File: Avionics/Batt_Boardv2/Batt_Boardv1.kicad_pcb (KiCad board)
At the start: 2 copper layers, 43 parts, among them J3 Screw_Terminal_01x01, J4 JST_PH_S2B-PH-SM4, J5 Screw_Terminal_01x02, J6 Screw_Terminal_01x02, J7 Screw_Terminal_01x02, J8 Screw_Terminal_01x02, Q1 IRF7458, Q2 IRF7458, U3 TMP36xS

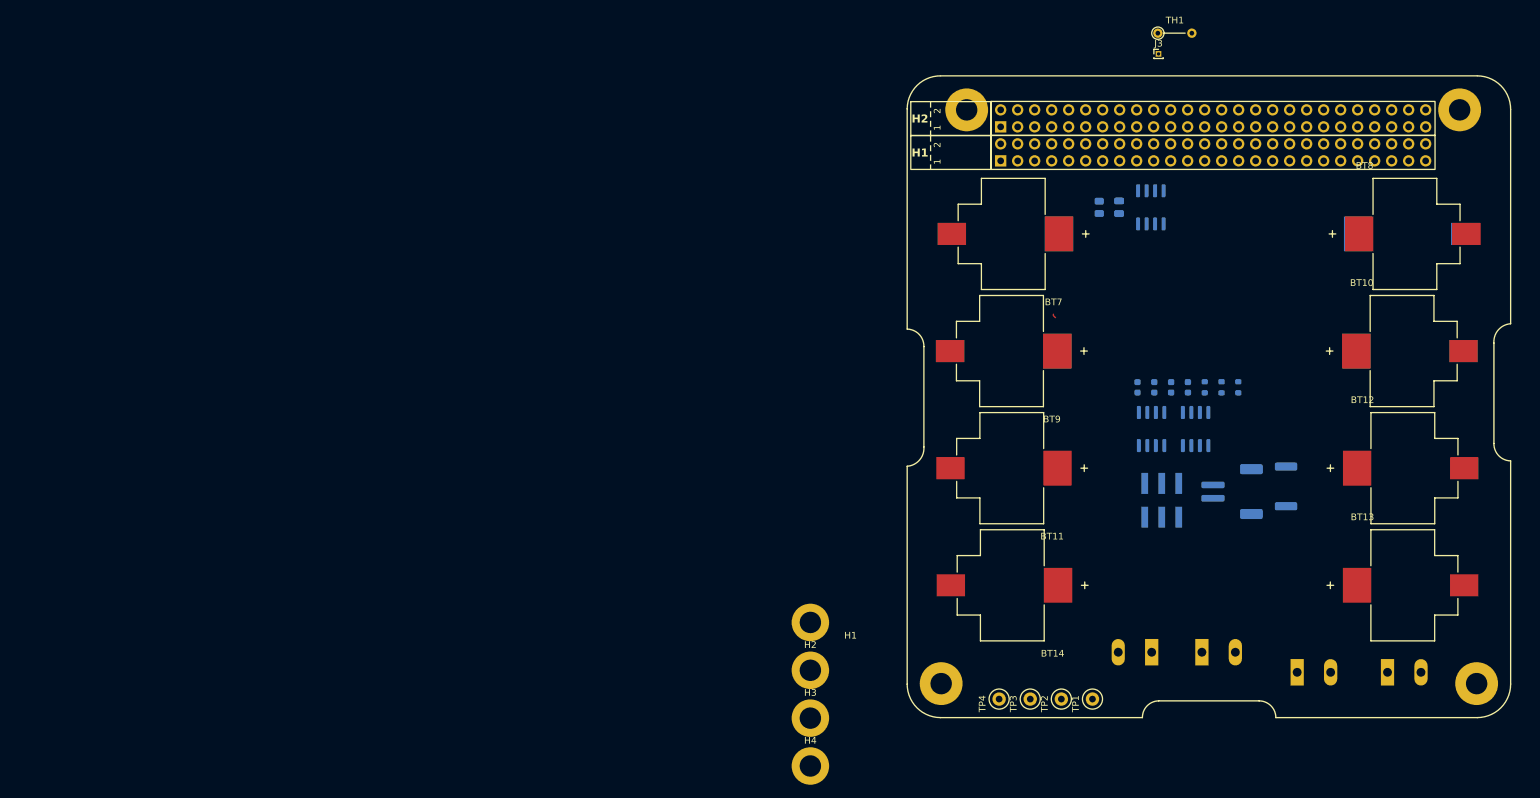
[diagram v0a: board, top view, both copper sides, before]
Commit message: 12/3/2024, Sephora Poteau: changed PC104 layout to include copper layer and edge cuts, and changed placement of components on Batt_Boardv2
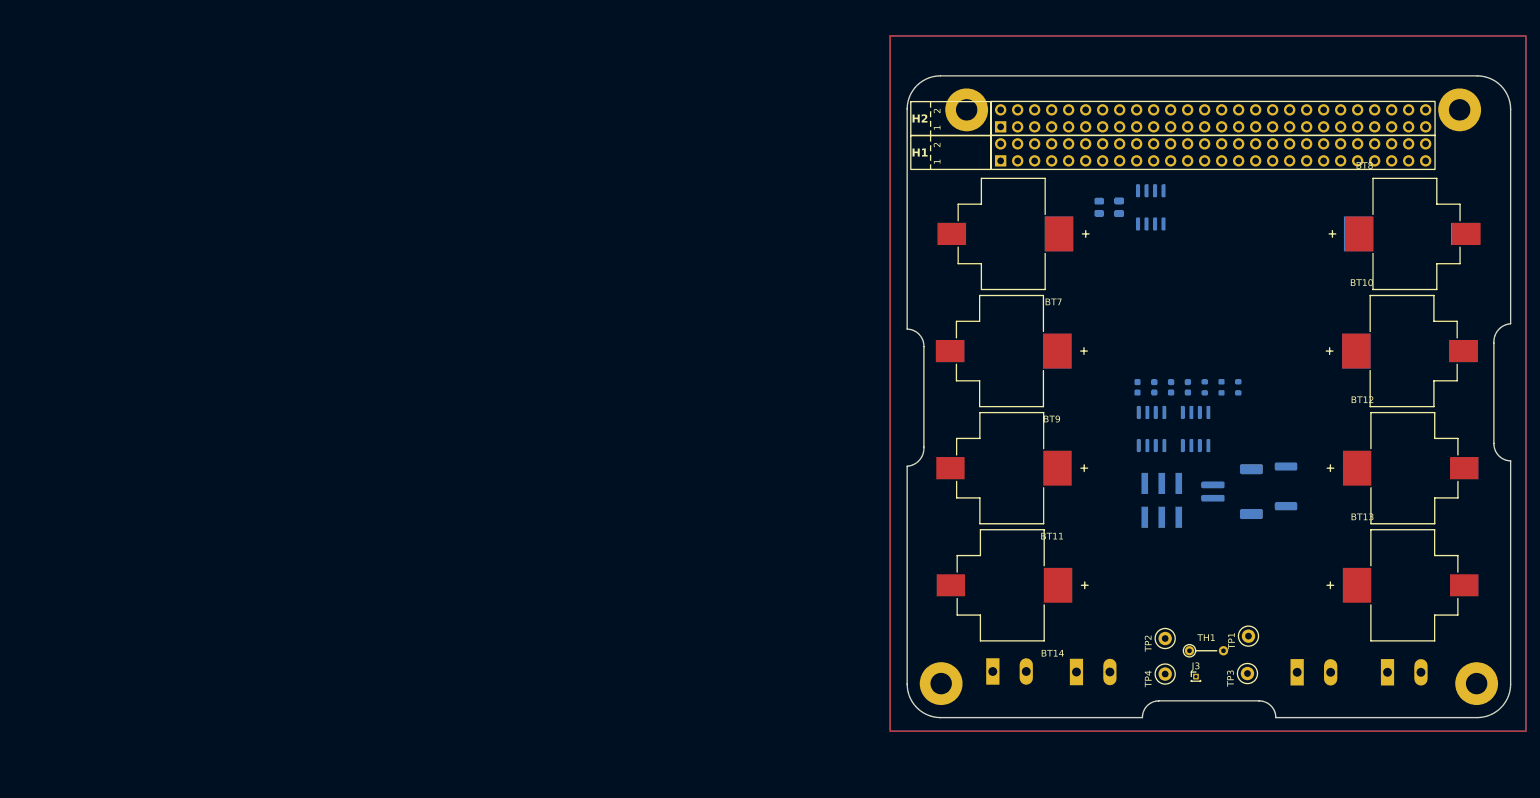
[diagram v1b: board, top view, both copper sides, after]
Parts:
- removed H1, H2, H3, H4: MountingHole_Pad, MountingHole:MountingHole_3.2mm_M3_DIN965_Pad
- moved J3 93.2 mm to (207.1, 139.1)
- moved TH1 92.4 mm to (206.1, 135.3)
- moved TP3 32.7 mm to (214.8, 138.7)
- moved TP1 25.1 mm to (215.0, 133.1)
- moved TP4 25.1 mm to (202.5, 138.8)
- moved J5 23.9 mm to (176.8, 138.4), turned to 0 degrees
- moved J8 19.0 mm to (189.3, 138.5)
- moved TP2 18.0 mm to (202.5, 133.5)
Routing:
- net (no net): track 1.56 -> 0.00 mm
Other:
- board outline added: 90.2 x 95.9 mm

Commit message: meeting
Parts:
- removed D1: TEMP_PWR, LED_SMD:LED_0805_2012Metric
- removed J3: Screw_Terminal_01x01, Connector_PinHeader_1.00mm:PinHeader_1x01_P1.00mm_Vertical
- removed J4: JST_PH_S2B-PH-SM4, Connector_JST:JST_PH_S2B-PH-SM4-TB_1x02-1MP_P2.00mm_Horizontal
- removed J5, J6, J7, J8: Screw_Terminal_01x02, TerminalBlock:TerminalBlock_Altech_AK300-2_P5.00mm
- removed R2: 15, Resistor_SMD:R_0805_2012Metric
- removed R5460N233AF1: ~, Connector_PinHeader_2.54mm:PinHeader_2x03_P2.54mm_Vertical_SMD
- removed TH1: Thermistor, Resistor_THT:R_Axial_DIN0204_L3.6mm_D1.6mm_P5.08mm_Vertical
- added S-8252: ~, Package_TO_SOT_SMD:SOT-23-5, B.Cu at (200.3, 121.3)
- C1, C3, C4, C5: footprint Capacitor_SMD:C_0603_1608Metric -> Capacitor_SMD:C_0805_2012Metric
- R1: footprint Resistor_SMD:R_2512_6332Metric -> Package_TO_SOT_SMD:TO-263-2
- R4, R5: footprint Resistor_SMD:R_0603_1608Metric -> Resistor_SMD:R_0805_2012Metric
- moved U3 63.1 mm to (195.9, 132.0)
- moved C2 61.9 mm to (204.8, 130.3)
- moved TP1 20.4 mm to (233.5, 141.5)
- moved TP2 19.7 mm to (184.5, 141.5)
- moved TP3 10.1 mm to (224.5, 141.5)
- moved C1 9.15 mm to (195.8, 104.7)
- moved C3 9.15 mm to (198.3, 104.7)
- moved C4 9.15 mm to (200.8, 104.7)
- moved C5 9.15 mm to (203.3, 104.7)
- moved Q1 9.15 mm to (197.9, 110.9)
- moved Q2 9.15 mm to (204.5, 110.9)
- moved R3 9.15 mm to (205.8, 104.7)
- moved R4 9.15 mm to (208.4, 104.7)
- moved R5 9.15 mm to (210.9, 104.7)
- moved TP4 8.94 mm to (194.0, 141.5)
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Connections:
- C1 pad 2: /Pack - -> GND
- C2 pad 1: Net-(D1-A) -> /3V3
- Q2 pad 1: /Pack - -> GND
- Q2 pad 2: /Pack - -> GND
- Q2 pad 3: /Pack - -> GND
- R3 pad 2: /Pack - -> GND
- TP3 pad 1: /Pack - -> GND
- TP4 pad 1: /Pack + -> /BATT_CS
- U1 pad 10: unconnected-(U1-Pad10) -> /BATT_CS
- U1 pad 11: unconnected-(U1-Pad11) -> /BATT_CS
- U1 pad 12: unconnected-(U1-BGLBON_RST-Pad12) -> /BATT_CS
- U1 pad 53: /batt_board_temp -> unconnected-(U1-TEMP_1-Pad53)
- U1 pad 57: unconnected-(U1-TEMP_7-Pad57) -> /batt_board_temp
- U1 pad 79: unconnected-(U1-3V3_MAIN-Pad79) -> /3V3
- U1 pad 80: unconnected-(U1-3V3_MAIN-Pad80) -> /3V3
- U1 pad 81: unconnected-(U1-GND-Pad81) -> GND
- U1 pad 82: unconnected-(U1-GND-Pad82) -> GND
- U1 pad 83: unconnected-(U1-GND-Pad83) -> GND
- U1 pad 84: unconnected-(U1-GND-Pad84) -> GND
- U1 pad 9: unconnected-(U1-Pad9) -> /BATT_CS
- U3 pad 5: Net-(D1-A) -> /3V3
- U3 pad 8: Net-(D1-A) -> /3V3

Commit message: feat: batt & PDU progress
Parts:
- removed BT10, BT11, BT12, BT13, BT14, BT15, BT17, BT18, BT7, BT8, BT9: 54, Battery 54:BAT_254TR
- removed U1: ~, PC104:PC104ConnectorFootprint (1)
- added BT1: 54, 254:BAT_254_1, B.Cu at (75.2, 68.1)
- added BT2: 54, 254:BAT_254_1, B.Cu at (75.2, 86.4)
- added BT3: 54, 254:BAT_254_1, B.Cu at (75.2, 104.8)
- added BT4: 54, 254:BAT_254_1, B.Cu at (74.9, 123.2)
- added BT5: 54, 254:BAT_254_1, F.Cu at (75.9, 68.1)
- added G***: LOGO, LOGO, F.Cu at (100.8, 129.9)
- added H1: MountingHole, MountingHole:MountingHole_3.2mm_M3_Pad_TopBottom, F.Cu at (39.4, 47.0)
- added H2: MountingHole, MountingHole:MountingHole_3.2mm_M3_Pad_TopBottom, F.Cu at (113.0, 47.0)
- added H3: MountingHole, MountingHole:MountingHole_3.2mm_M3_Pad_TopBottom, F.Cu at (115.6, 132.7)
- added H4: MountingHole, MountingHole:MountingHole_3.2mm_M3_Pad_TopBottom, F.Cu at (35.6, 132.7)
- added J1: Conn_02x26_Odd_Even, Connector_PinHeader_2.54mm:PinHeader_2x26_P2.54mm_Vertical, F.Cu at (44.5, 54.6)
- added J2: Conn_02x26_Odd_Even, Connector_PinHeader_2.54mm:PinHeader_2x26_P2.54mm_Vertical, F.Cu at (44.5, 49.5)
- BT16: footprint Battery 54:BAT_254TR -> 254:BAT_254_1; moved to F.Cu
- C1, C2, C3, C4, C5, Q1, Q2, R1, R3, R4, R5, S-8252, U3: moved to F.Cu
- moved TP1 188.2 mm to (45.4, 134.1)
- moved TP3 170.3 mm to (54.4, 134.1)
- moved R5 156.8 mm to (54.2, 101.2)
- moved R4 151.7 mm to (56.7, 101.2)
- moved C2 150.3 mm to (54.6, 124.0)
- moved R3 146.7 mm to (59.2, 101.2)
- moved Q2 144.0 mm to (60.5, 107.4)
- moved C5 141.7 mm to (61.7, 101.2)
- moved C4 136.7 mm to (64.2, 101.2)
- moved S-8252 135.6 mm to (64.7, 117.8), turned to 0 degrees
- moved TP4 134.0 mm to (60.2, 133.8)
- moved R1 132.7 mm to (87.9, 112.0)
- moved U3 132.5 mm to (63.5, 125.7)
- moved C3 131.7 mm to (66.7, 101.2)
- moved Q1 130.8 mm to (67.1, 107.4)
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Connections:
- net GND renamed GNDREF
- R5 pad 1: /BATT_CS -> /BATT_PRE_INH
- TP4 pad 1: /BATT_CS -> /BATT_PRE_INH
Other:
- outline, holes or cut-outs redrawn
- board text added: "AVIONICS"
- board text added: "PULSE-A"
- board text added: "battery pack"
- board text added: "rev. 2.0.0, XX.YY.ZZ"

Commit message: fix: battery format
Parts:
- moved BT3 38.2 mm to (76.0, 66.7), turned to 0 degrees
- moved BT1 35.6 mm to (75.2, 103.7)
- moved BT5 1.46 mm to (75.9, 66.6)
- moved BT16 1.36 mm to (75.2, 85.3), turned to 180 degrees
- moved BT4 1.34 mm to (76.0, 122.3), turned to 0 degrees
- moved BT2 1.24 mm to (75.2, 85.2)

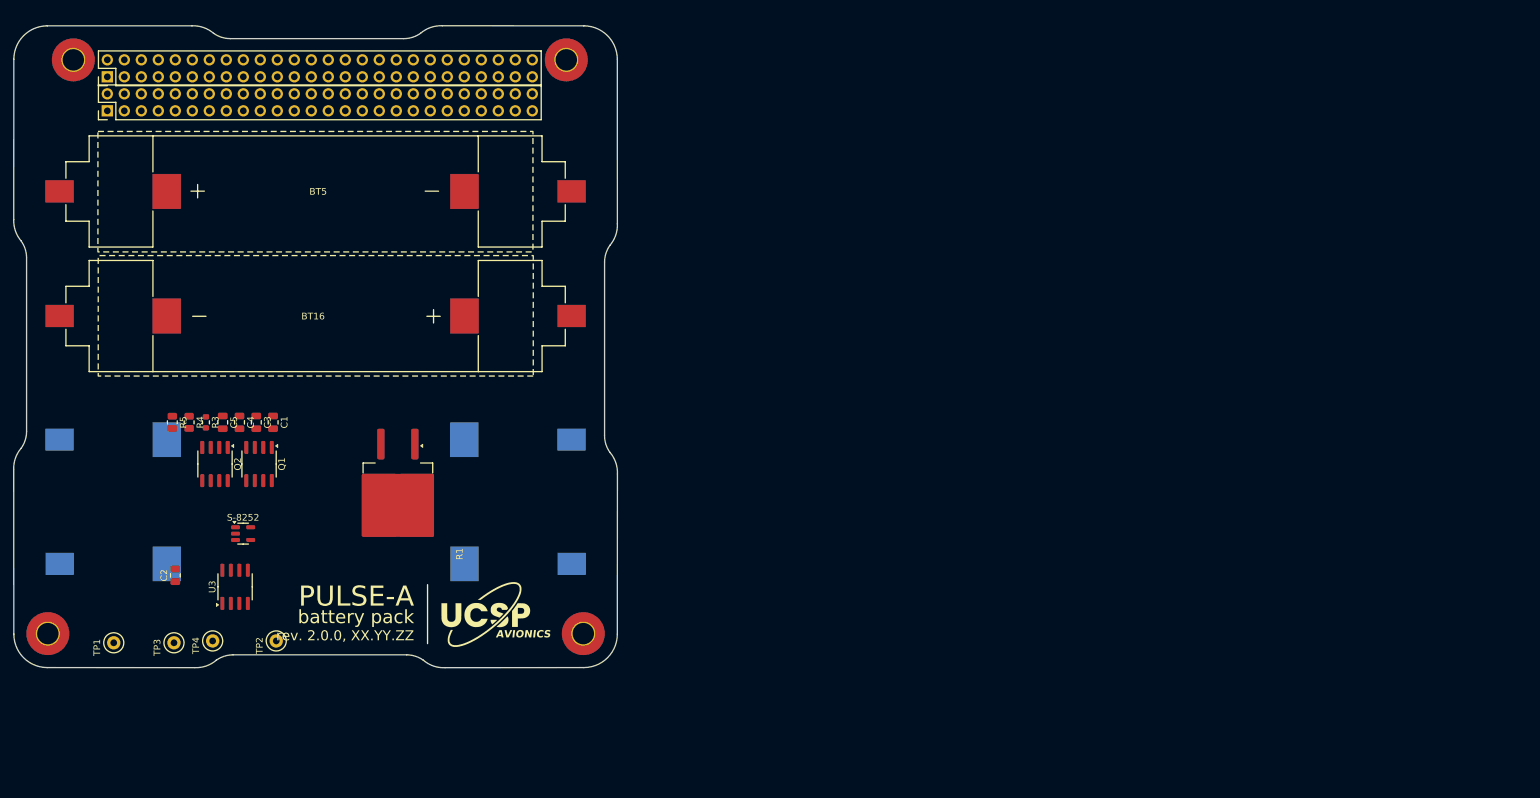
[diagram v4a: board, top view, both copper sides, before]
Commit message: 12/5/2024, Sephora Poteau: Changed Layout of BattBoardPCB to lay traces
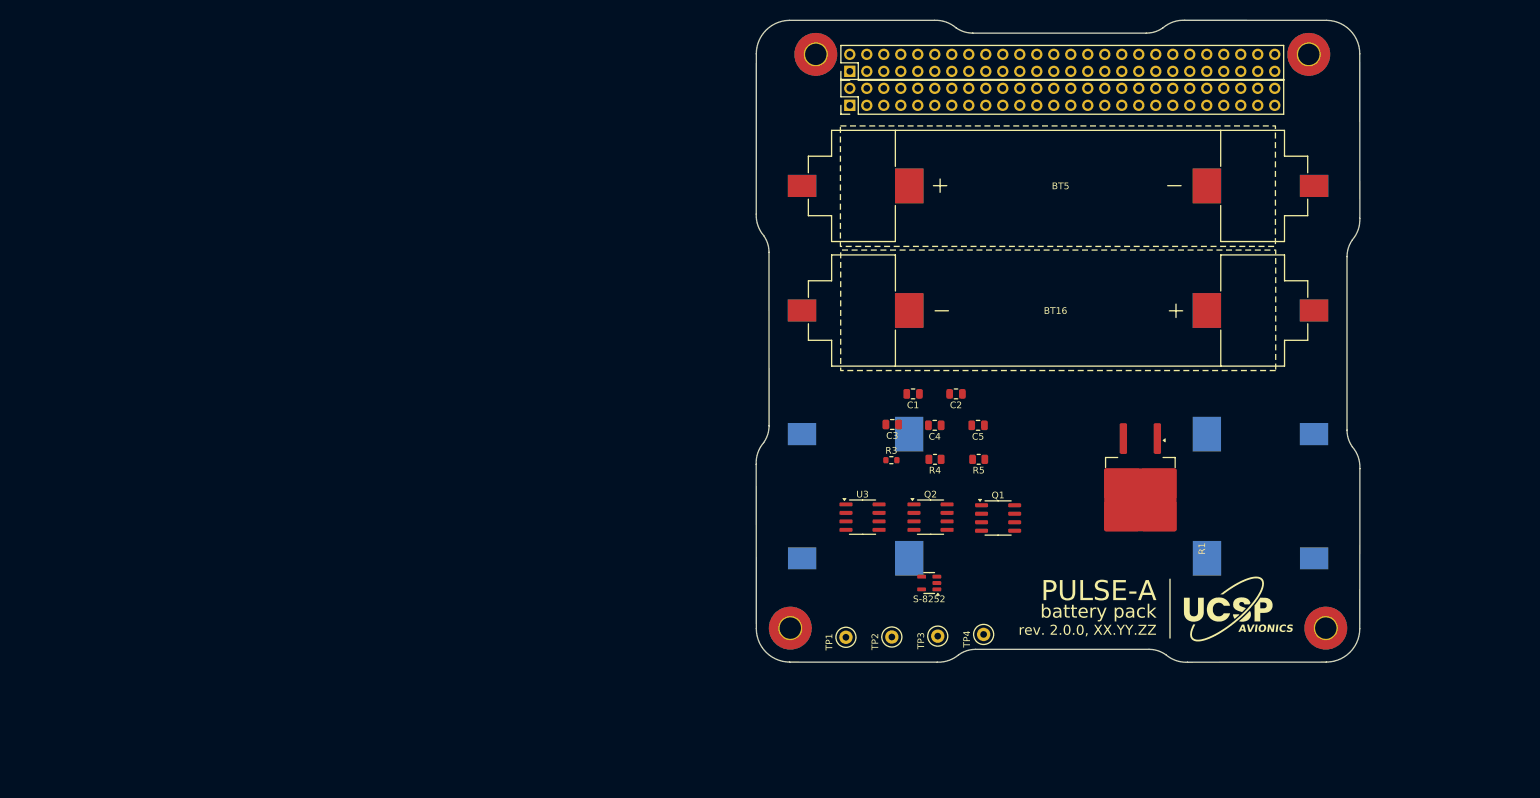
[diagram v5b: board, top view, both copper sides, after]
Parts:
- moved R5 120.6 mm to (174.6, 106.7), turned to 180 degrees
- moved C2 119.8 mm to (171.3, 96.9), turned to 180 degrees
- moved TP4 115.2 mm to (175.4, 132.8)
- moved TP3 114.1 mm to (168.5, 133.1)
- moved C5 112.9 mm to (174.6, 101.6), turned to 180 degrees
- moved R4 111.6 mm to (168.1, 106.7), turned to 180 degrees
- moved G*** 110.9 mm to (211.7, 129.1)
- moved BT16 110.9 mm to (186.1, 84.5)
- moved BT3 110.9 mm to (186.9, 65.9)
- moved BT5 110.9 mm to (186.9, 65.8)
- moved H1 110.9 mm to (150.3, 46.2)
- moved H2 110.9 mm to (224.0, 46.2)
- moved H3 110.9 mm to (226.5, 131.9)
- moved H4 110.9 mm to (146.5, 131.9)
- moved BT1 110.9 mm to (186.1, 102.9)
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
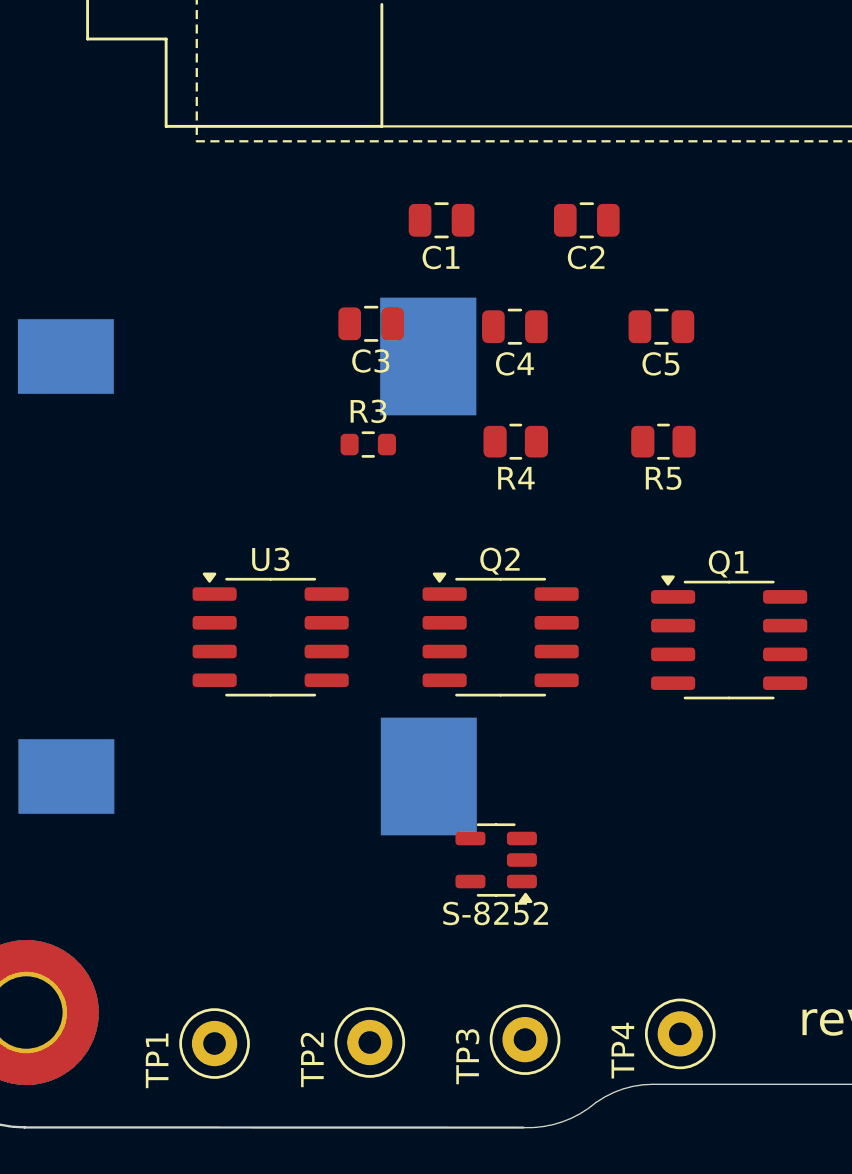
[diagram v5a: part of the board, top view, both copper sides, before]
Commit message: 12/5/2024, Sephora Poteau: Capasitors and Resistors have been traced, need to trace rest of board
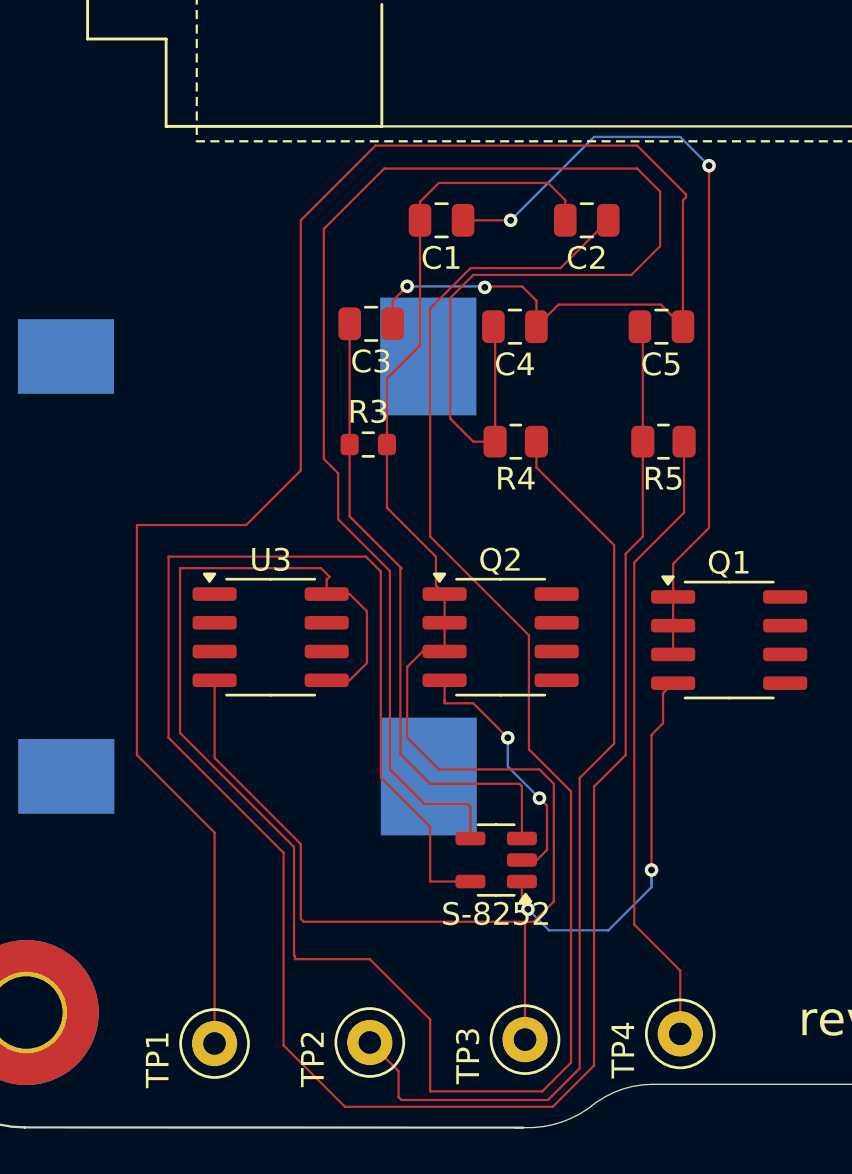
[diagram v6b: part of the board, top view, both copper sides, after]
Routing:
- net /VDD: track 0.00 -> 98.9 mm
- net /3V3: track 0.00 -> 95.9 mm
- net /B-: track 0.00 -> 85.3 mm, vias 0 -> 2
- net GNDREF: track 0.00 -> 76.0 mm
- net Net-(S-8252-VC): track 0.00 -> 72.6 mm
- net /BM: track 0.00 -> 41.3 mm
- net Net-(C1-Pad1): track 0.00 -> 35.3 mm, vias 0 -> 2
- net Net-(S-8252-V-): track 0.00 -> 28.2 mm
- net /BATT_PRE_INH: track 0.00 -> 27.9 mm
- net Net-(Q1-G): track 0.00 -> 18.1 mm, vias 0 -> 2
- net Net-(Q2-G): track 0.00 -> 11.4 mm, vias 0 -> 2
